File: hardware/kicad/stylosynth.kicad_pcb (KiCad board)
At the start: 2 copper layers, 200 x 120 mm, 101 parts, among them J1 9V DC (centre -), J2 9V BATT, J3 STYLUS, J4 PHONES, J5 SPEAKER, K1 KEYPAD, SW1 POWER, SW2 OCT -1, SW3 OCT -2, SW4 TONE, SW5 VIBRATO, U1 LP2950-5.0, U2 TLC555, U3 CD4040, U4 LM386, U5 LM358

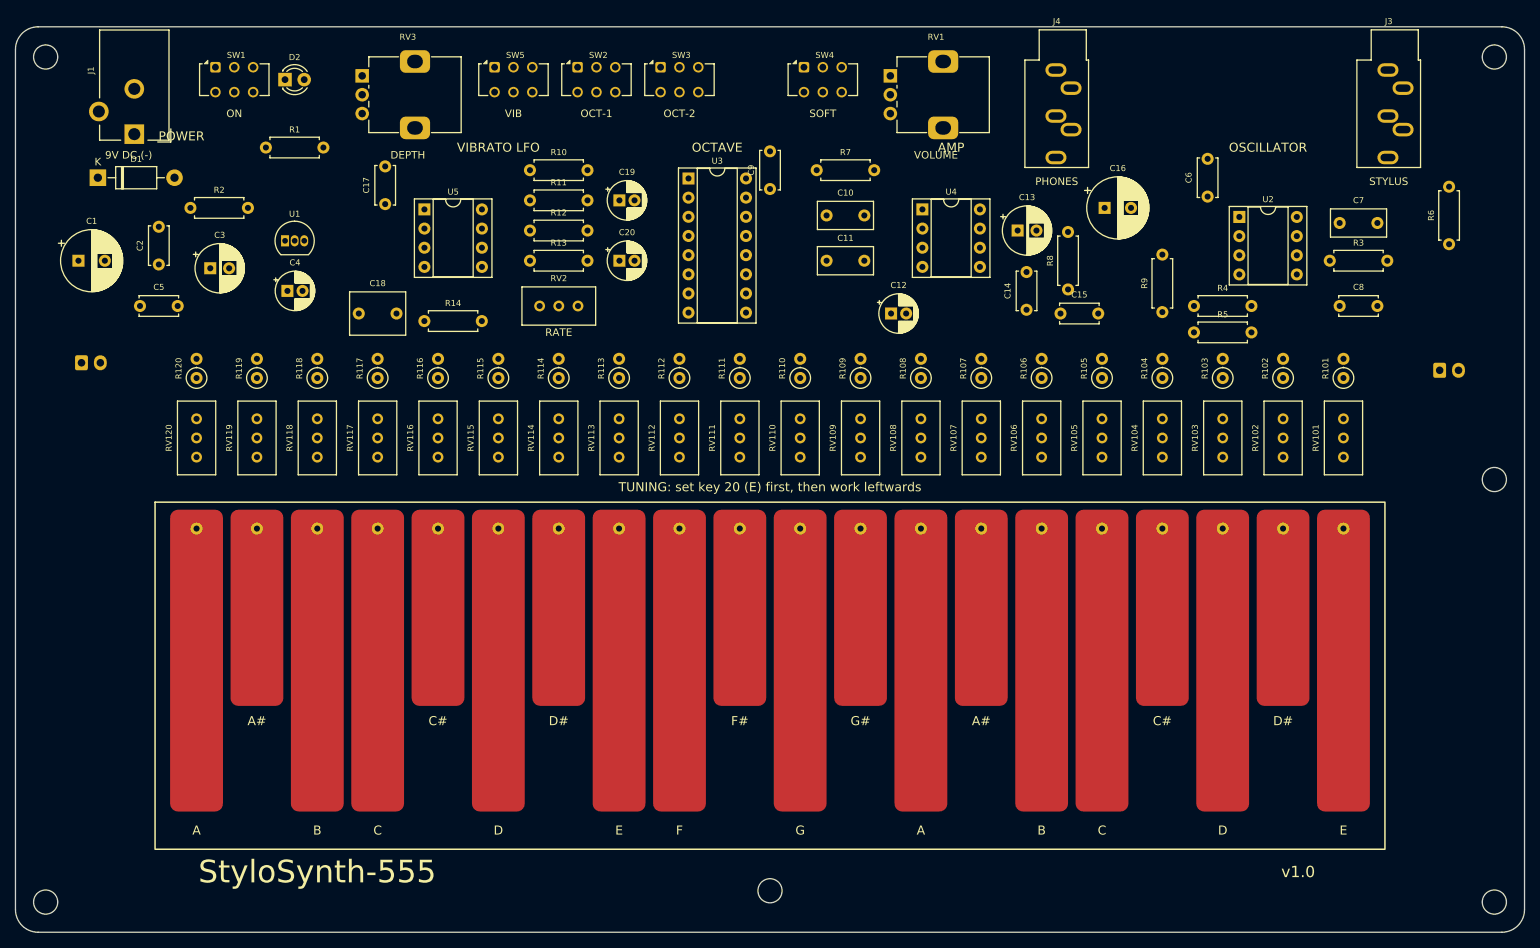
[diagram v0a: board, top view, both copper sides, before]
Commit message: v1.1: piano-layout keyboard, fixed E96 ladder with TUNE/SPAN calibration, 170x108 board
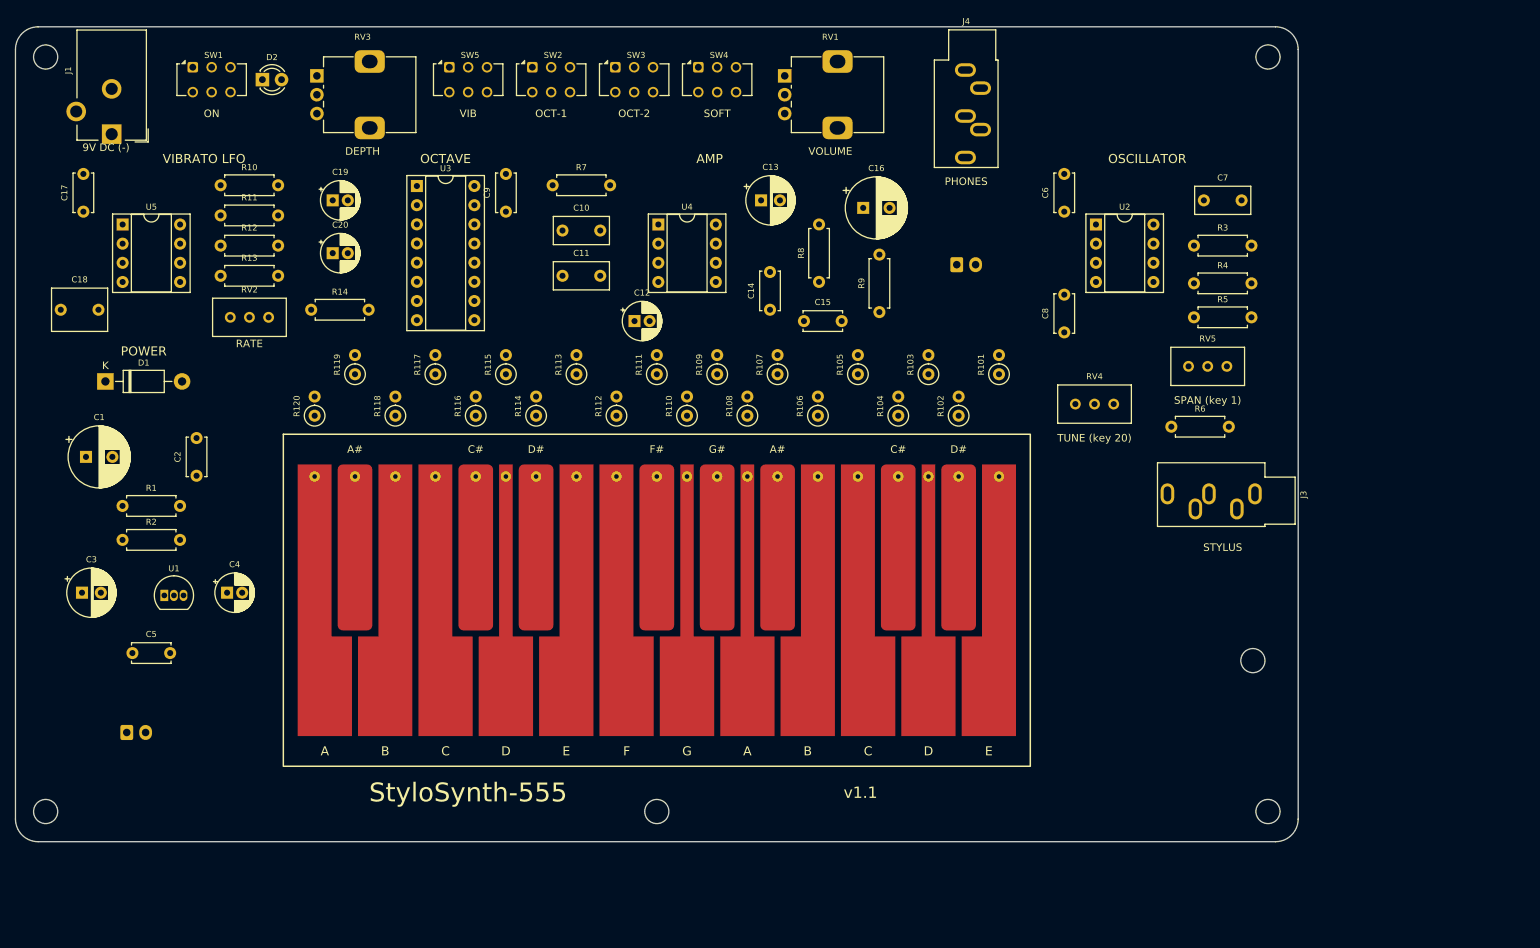
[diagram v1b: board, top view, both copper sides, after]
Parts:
- removed RV101: 5k, Potentiometer_THT:Potentiometer_Bourns_3296W_Vertical
- removed RV102, RV103, RV104, RV105, RV106, RV107, RV108, RV109, RV110, RV111, RV112, RV113, RV114, RV115, RV116, RV117, RV118, RV119, RV120: 1k, Potentiometer_THT:Potentiometer_Bourns_3296W_Vertical
- added RV4: 2k, Potentiometer_THT:Potentiometer_Bourns_3296W_Vertical, F.Cu at (195.6, 90.0)
- added RV5: 1k, Potentiometer_THT:Potentiometer_Bourns_3296W_Vertical, F.Cu at (210.6, 85.0)
- R101: value 9.1k -> 11k3
- R102: value 220 -> 750
- R103: value 270 -> 787
- R104: value 300 -> 845
- R105: value 360 -> 887
- R106: value 430 -> 953
- R107: value 470 -> 1k
- R108: value 510 -> 1k05
- R109: value 560 -> 1k13
- R110: value 620 -> 1k18
- R111: value 680 -> 1k27
- R112: value 750 -> 1k33
- R113: value 820 -> 1k4
- R114: value 910 -> 1k5
- R115: value 1k -> 1k58
- R116: value 1.1k -> 1k69
- R117: value 1.2k -> 1k78
- R118: value 1.3k -> 1k87
- R119: value 1.3k -> 2k
- R120: value 1.5k -> 2k15
- R5: value 3k -> 2k4
- moved J5 65.5 mm to (174.8, 71.5)
- moved K1 63.3 mm to (87.0, 98.0)
- moved J3 58.9 mm to (214.3, 101.9), turned to -90 degrees
- moved R1 51.2 mm to (64.2, 103.5)
- moved U1 49.6 mm to (69.7, 115.4)
- moved J2 49.4 mm to (64.8, 133.5)
- moved C3 46.2 mm to (58.8, 115.0)
- moved C5 46.0 mm to (65.5, 123.0)
- moved R101 45.7 mm to (180.3, 86.0)
- moved R2 44.9 mm to (64.2, 108.0)
- moved R6 44.0 mm to (203.2, 93.0), turned to 0 degrees
- moved R102 43.3 mm to (175.0, 91.5)
- moved R10 41.0 mm to (77.2, 61.0)
- moved R11 41.0 mm to (77.2, 65.0)
- moved R12 41.0 mm to (77.2, 69.0)
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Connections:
- R102 pad 2: LAD1 -> KEY19
- R103 pad 2: LAD2 -> KEY18
- R104 pad 2: LAD3 -> KEY17
- R105 pad 2: LAD4 -> KEY16
- R106 pad 2: LAD5 -> KEY15
- R107 pad 2: LAD6 -> KEY14
- R108 pad 2: LAD7 -> KEY13
- R109 pad 2: LAD8 -> KEY12
- R110 pad 2: LAD9 -> KEY11
- R111 pad 2: LAD10 -> KEY10
- R112 pad 2: LAD11 -> KEY9
- R113 pad 2: LAD12 -> KEY8
- R114 pad 2: LAD13 -> KEY7
- R115 pad 2: LAD14 -> KEY6
- R116 pad 2: LAD15 -> KEY5
- R117 pad 2: LAD16 -> KEY4
- R118 pad 2: LAD17 -> KEY3
- R119 pad 2: LAD18 -> KEY2
- R120 pad 2: LAD19 -> KEY1
- R5 pad 2: GND -> CV_LO
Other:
- board size 200 x 120 mm -> 170 x 108 mm
- board text added: "SPAN (key 1)"
- board text added: "TUNE (key 20)"
- board text added: "v1.1"
- board text removed: "TUNING: set key 20 (E) first, then work leftwards"
- board text removed: "v1.0"

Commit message: v1.2: compact 136x98 layout, vertical resistors, single ladder row
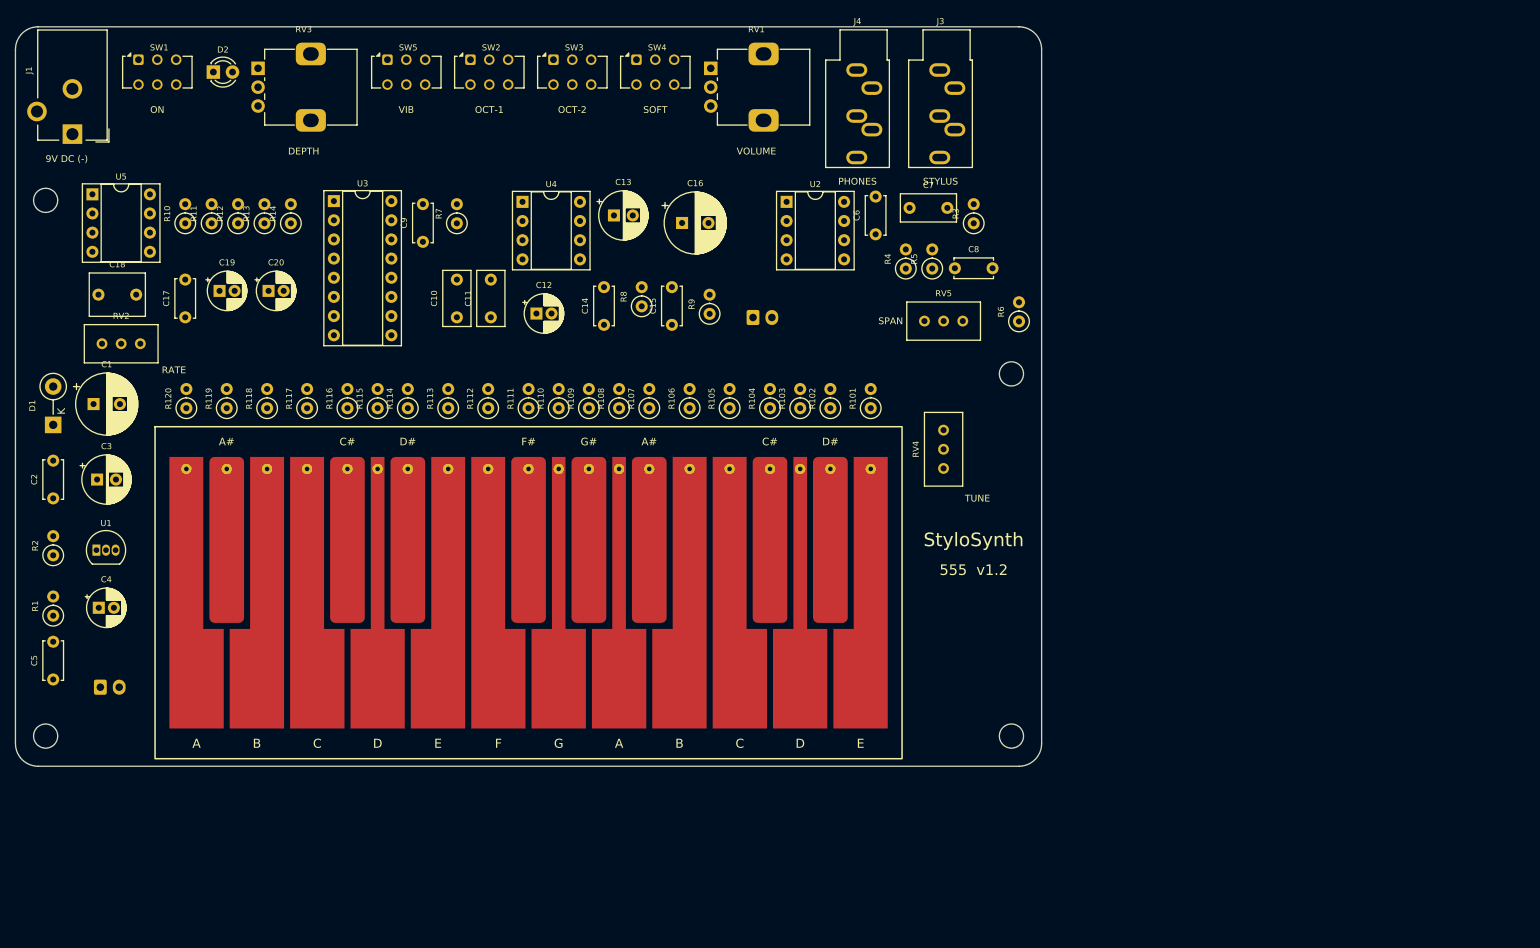
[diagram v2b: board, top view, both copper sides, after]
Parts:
- removed H5, H6: M3, MountingHole:MountingHole_3.2mm_M3
- D1: footprint Diode_THT:D_DO-41_SOD81_P10.16mm_Horizontal -> Diode_THT:D_DO-41_SOD81_P5.08mm_Vertical_KathodeUp
- R1, R10, R11, R12, R13, R14, R2, R3, R4, R5, R6, R7, R8, R9: footprint Resistor_THT:R_Axial_DIN0207_L6.3mm_D2.5mm_P7.62mm_Horizontal -> Resistor_THT:R_Axial_DIN0207_L6.3mm_D2.5mm_P2.54mm_Vertical
- moved J3 70.0 mm to (172.5, 45.7), turned to 0 degrees
- moved H2 54.0 mm to (182.0, 86.0)
- moved U2 41.1 mm to (152.2, 63.2)
- moved C7 39.0 mm to (168.5, 64.0)
- moved R4 38.2 mm to (168.0, 72.0), turned to 90 degrees
- moved RV5 35.5 mm to (175.6, 79.0)
- moved H4 35.4 mm to (182.0, 134.0)
- moved R5 35.3 mm to (171.5, 72.0), turned to 90 degrees
- moved R3 29.3 mm to (177.0, 66.0), turned to 90 degrees
- moved J5 27.9 mm to (147.8, 78.5)
- moved C6 25.2 mm to (164.0, 67.5)
- moved R6 24.5 mm to (183.0, 79.0), turned to 90 degrees
- moved C16 24.1 mm to (138.3, 66.0)
- moved R8 23.7 mm to (133.0, 77.0)
- moved RV4 22.8 mm to (173.0, 93.5), turned to 90 degrees
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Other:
- board size 170 x 108 mm -> 136 x 98 mm
- board text added: "555 v1.2"
- board text added: "SPAN"
- board text added: "StyloSynth"
- board text added: "TUNE"
- board text removed: "AMP"
- board text removed: "OCTAVE"
- board text removed: "OSCILLATOR"
- board text removed: "POWER"
- board text removed: "SPAN (key 1)"
- board text removed: "StyloSynth-555"
- board text removed: "TUNE (key 20)"
- board text removed: "VIBRATO LFO"
- board text removed: "v1.1"

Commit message: Routed v1.2 board (DRC clean), enclosure geometry + Blender build scripts
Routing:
- net GND: track 0.00 -> 425.2 mm
- net +5V: track 0.00 -> 236.9 mm, vias 0 -> 1
- net +9V: track 0.00 -> 182.7 mm
- net CV: track 0.00 -> 102.3 mm
- net OSC_OUT: track 0.00 -> 99.6 mm, vias 0 -> 1
- net BAT_P: track 0.00 -> 87.5 mm
- net LED_A: track 0.00 -> 79.3 mm
- net VSW_IN: track 0.00 -> 55.0 mm
- net KEY20: track 0.00 -> 54.4 mm
- net OCT_Q2: track 0.00 -> 51.4 mm
- net KEY9: track 0.00 -> 50.1 mm
- net KEY8: track 0.00 -> 50.1 mm
- net KEY15: track 0.00 -> 50.0 mm
- net KEY3: track 0.00 -> 50.0 mm
- net KEY16: track 0.00 -> 50.0 mm
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- added copper zone on B.Cu, net GND
- added copper zone on F.Cu, net GND
